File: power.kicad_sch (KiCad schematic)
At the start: 0 parts

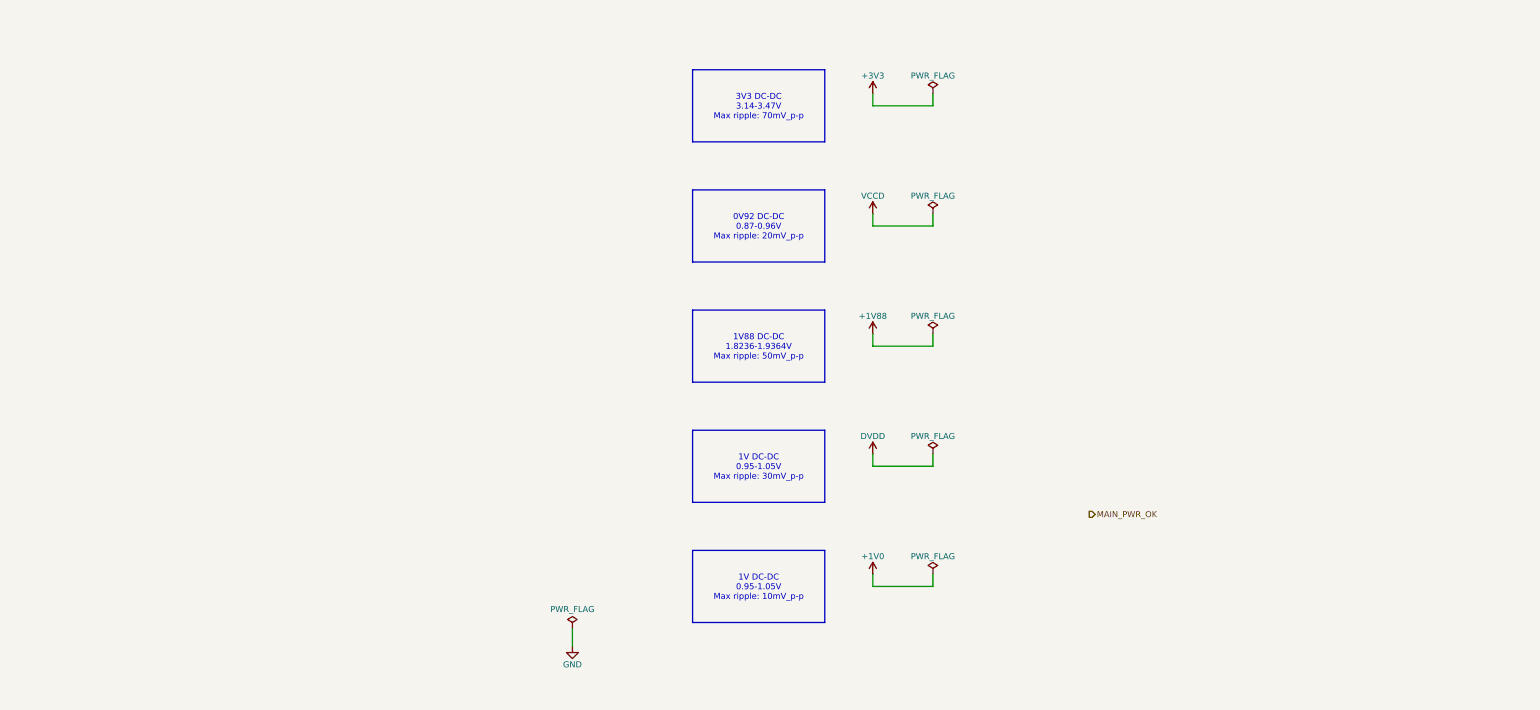
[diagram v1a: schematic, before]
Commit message: [#80813] Add power input connectors, heatsink, mounting, draft component placement
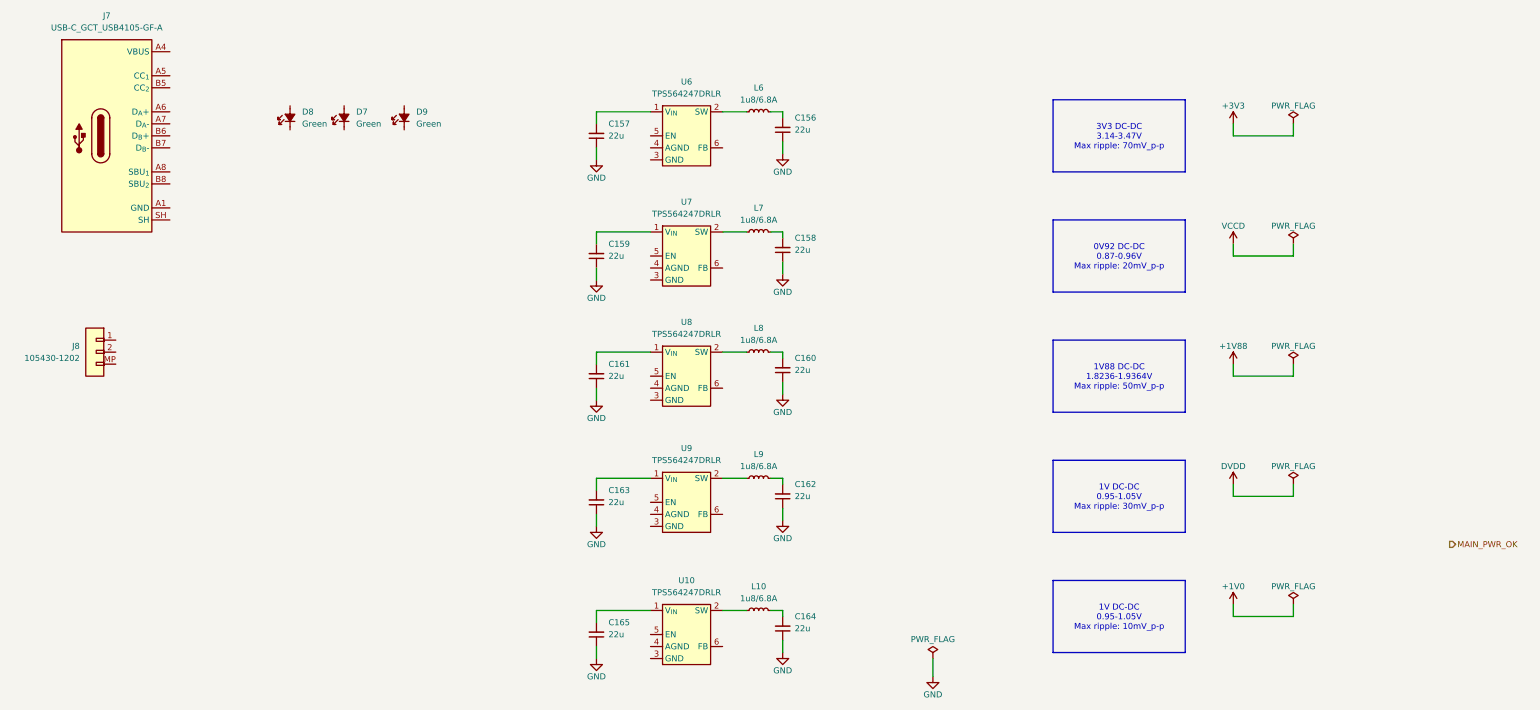
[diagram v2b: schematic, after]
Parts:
- added C156, C157, C158, C159, C160, C161, C162, C163, C164, C165: C_22u_16V_0603, antmicro-footprints:C_0603_1608Metric, symbol antmicroCapacitors0603:C_22u_16V_0603
- added D7, D8, D9: LED_G_0603_LG_L29K-G2J1-24-Z, antmicro-footprints:LED_0603_1608Metric_G, symbol antmicroLEDIndicationDiscrete:LED_G_0603_LG_L29K-G2J1-24-Z
- added J7: USB-C_GCT_USB4105-GF-A, antmicro-footprints:USB-C_Receptacle_GCT_USB4105-GF-A, symbol antmicroUSBConnectors:USB-C_GCT_USB4105-GF-A
- added J8: Molex_Nano-Fit_1x2_SMD_1054301202, antmicro-footprints:Conn_Molex_Nano-Fit_1x2_SMD_1054301202, symbol antmicroWire2BoardConnectors:Molex_Nano-Fit_1x2_SMD_1054301202
- added L10, L6, L7, L8, L9: L_1u8_6.8A_WE-MAPI-4020, antmicro-footprints:L_WE-MAPI-4020, symbol antmicroFixedInductors:L_1u8_6.8A_WE-MAPI-4020
- added U10, U6, U7, U8, U9: TPS564247DRLR, antmicro-footprints:SOT-563, symbol antmicroDCDCConverters:TPS564247DRLR
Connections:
- net GND: now also C156.1, C157.1, C158.1, C159.1, C160.1, C161.1, C162.1, C163.1, C164.1, C165.1
- new net: C156.2, L6.2
- new net: C162.2, L9.2
- new net: C165.2, U10.1 (V_{IN})
- new net: L10.1, U10.2 (SW)
- new net: L8.1, U8.2 (SW)
- new net: C160.2, L8.2
- new net: C159.2, U7.1 (V_{IN})
- new net: C161.2, U8.1 (V_{IN})
- new net: C157.2, U6.1 (V_{IN})
- new net: L6.1, U6.2 (SW)
- new net: L7.1, U7.2 (SW)
- new net: L9.1, U9.2 (SW)
- new net: C163.2, U9.1 (V_{IN})
- new net: C158.2, L7.2
- new net: C164.2, L10.2
- new net: J7.A1 (GND), J7.A12 (GND), J7.B1 (GND), J7.B12 (GND)
- new net: J7.A4 (VBUS), J7.A9 (VBUS), J7.B4 (VBUS), J7.B9 (VBUS)

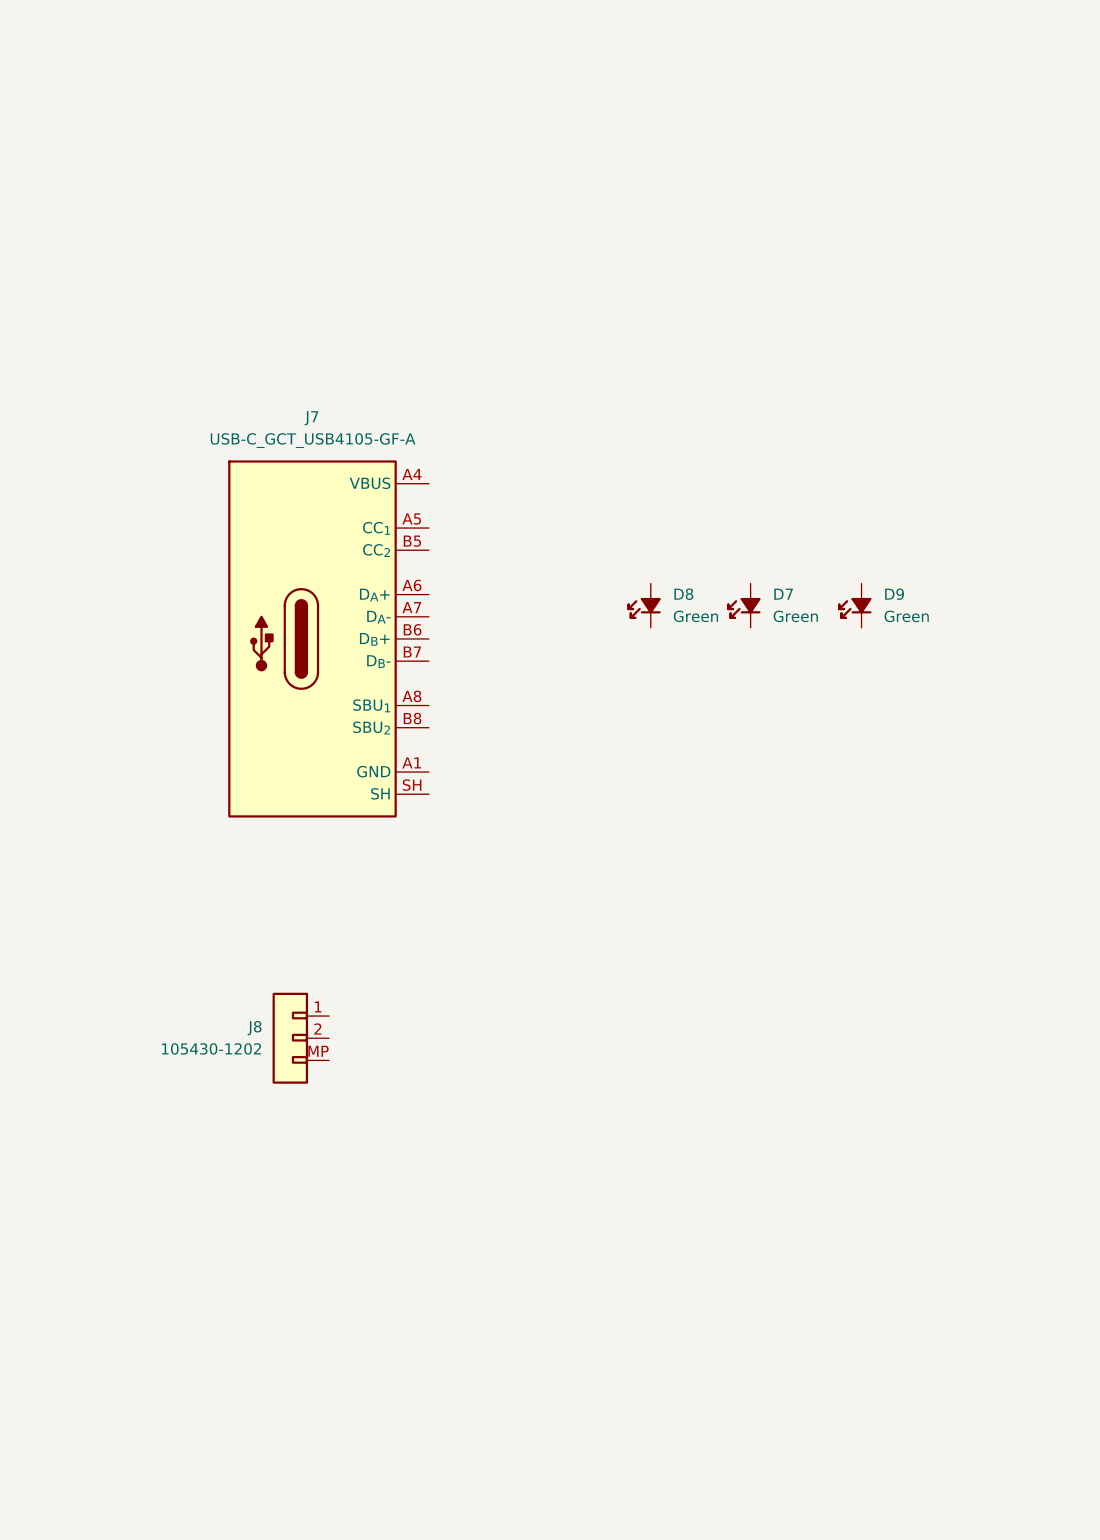
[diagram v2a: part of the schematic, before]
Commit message: [#80813] WIP: Connect USB-C connector
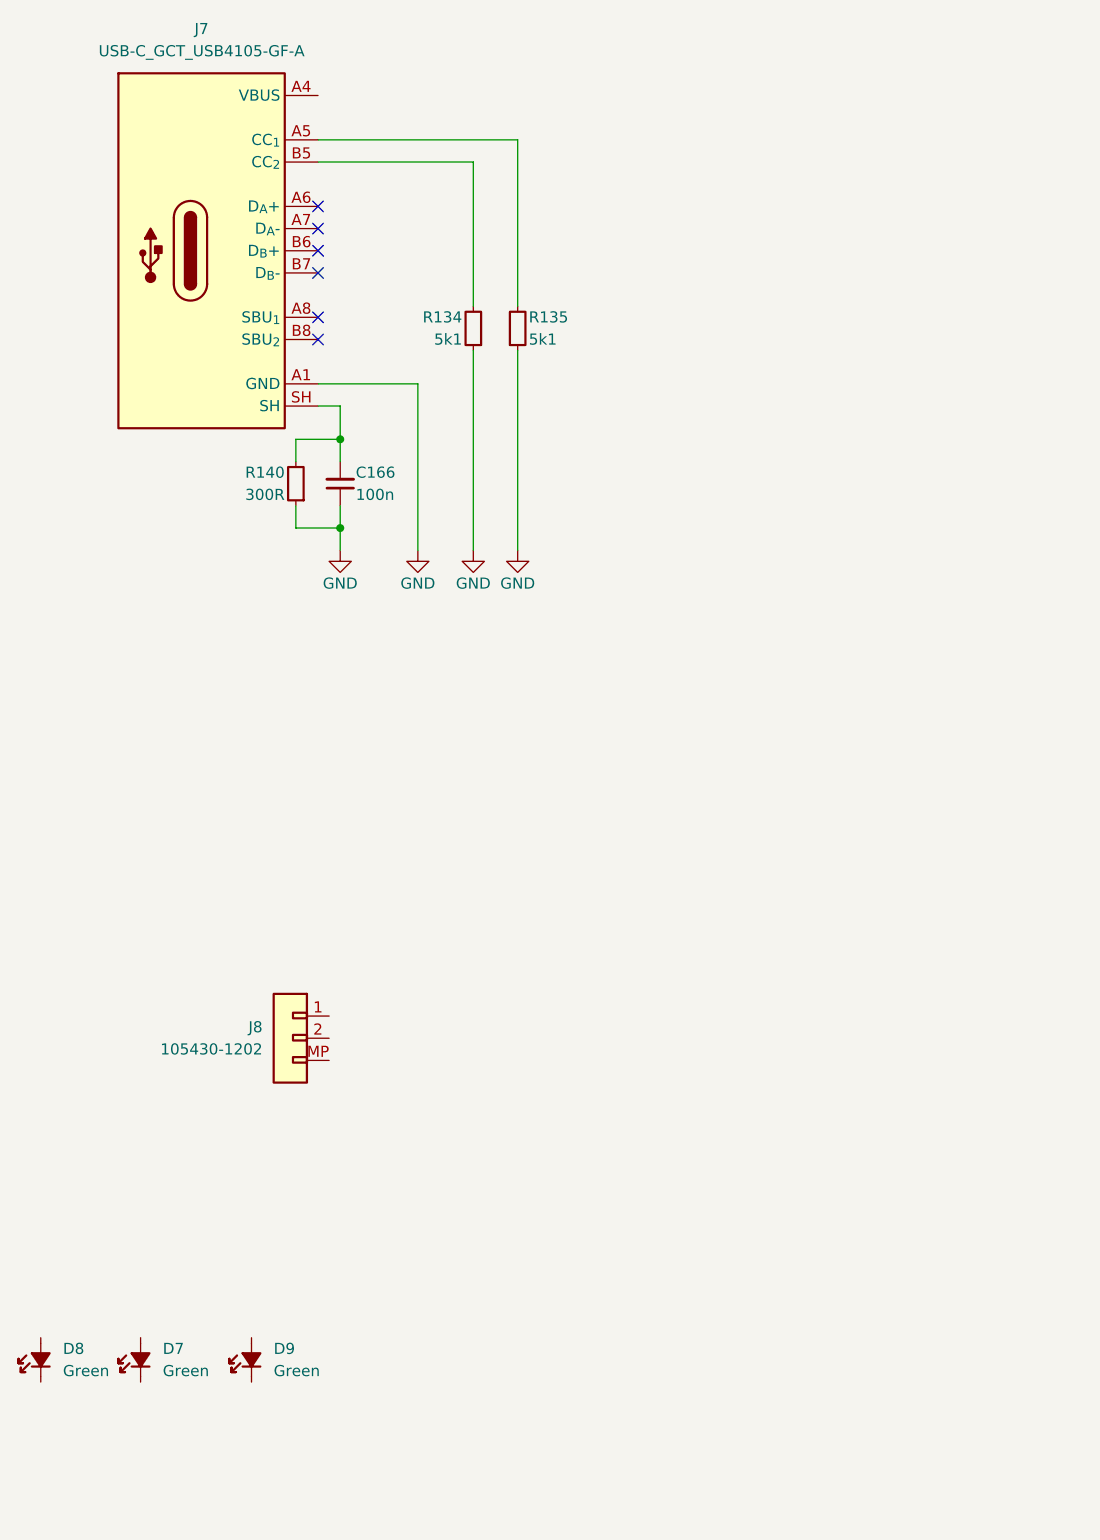
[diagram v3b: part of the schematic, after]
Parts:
- added C166: C_100n_16V_X7R_0402, antmicro-footprints:C_0402_1005Metric, symbol antmicroCapacitors0402:C_100n_16V_X7R_0402
- added R134, R135: R_5k1_0402, antmicro-footprints:R_0402_1005Metric, symbol antmicroResistors0402:R_5k1_0402
- added R140: R_300R_0402, antmicro-footprints:R_0402_1005Metric, symbol antmicroResistors0402:R_300R_0402
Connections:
- net GND: now also J7.A1 (GND), J7.A12 (GND), J7.B1 (GND), J7.B12 (GND), C166.1, R134.1, R135.1, R140.1
- net at J7.A5 (CC_{1}): now also R135.2
- net at J7.B5 (CC_{2}): now also R134.2
- net at J7.SH: now also C166.2, R140.2
- no-connect marks 0 -> 6
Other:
- moved on the sheet: D7, D8, D9, J7

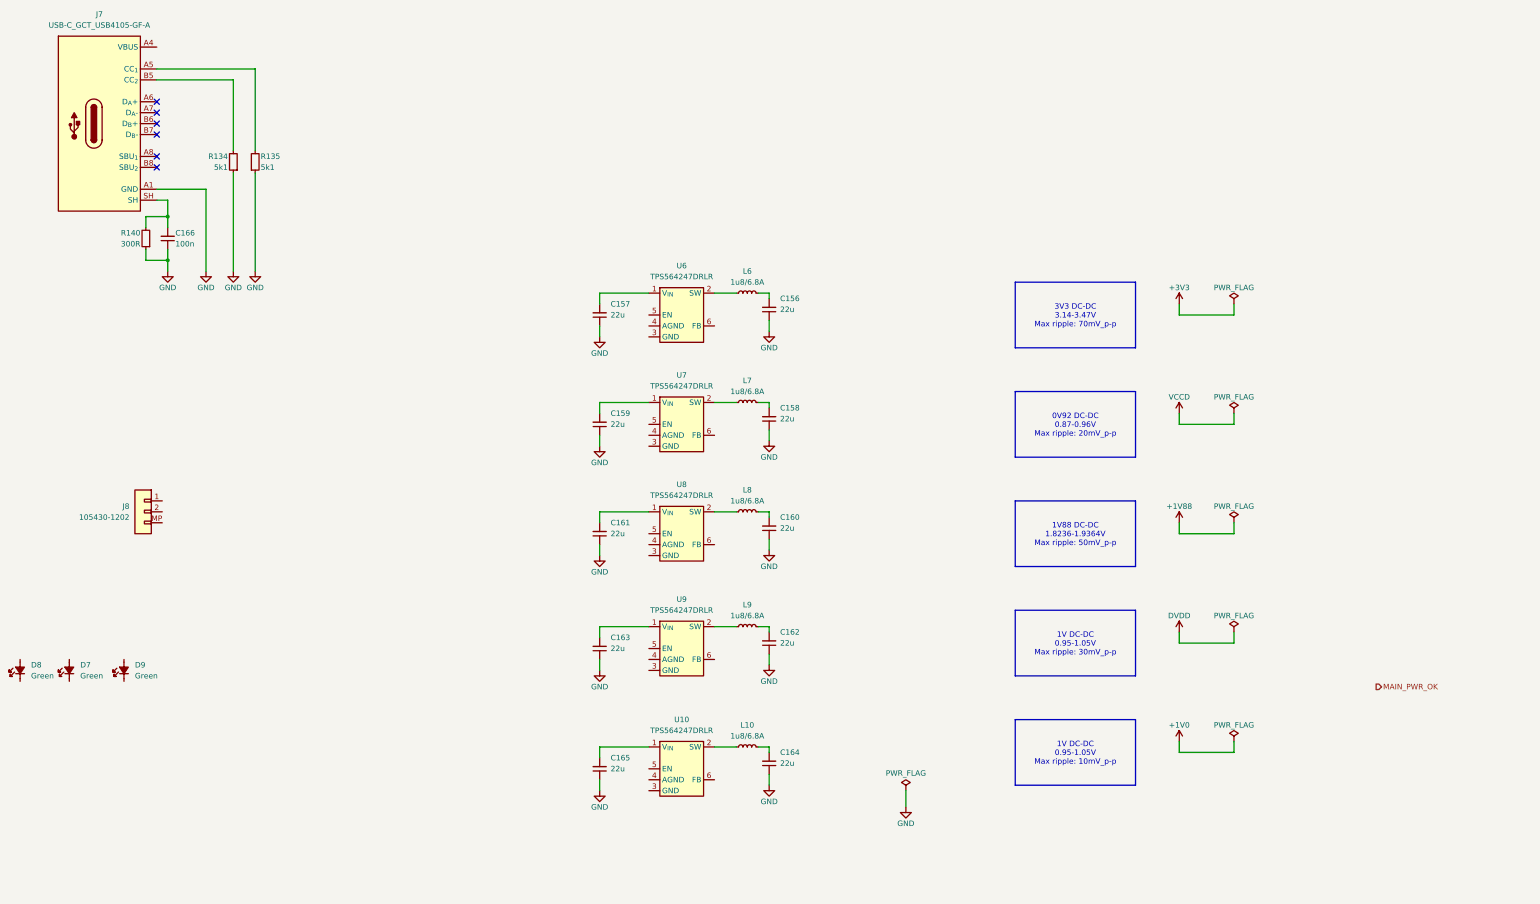
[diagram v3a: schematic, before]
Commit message: [#80813] Add power ORing
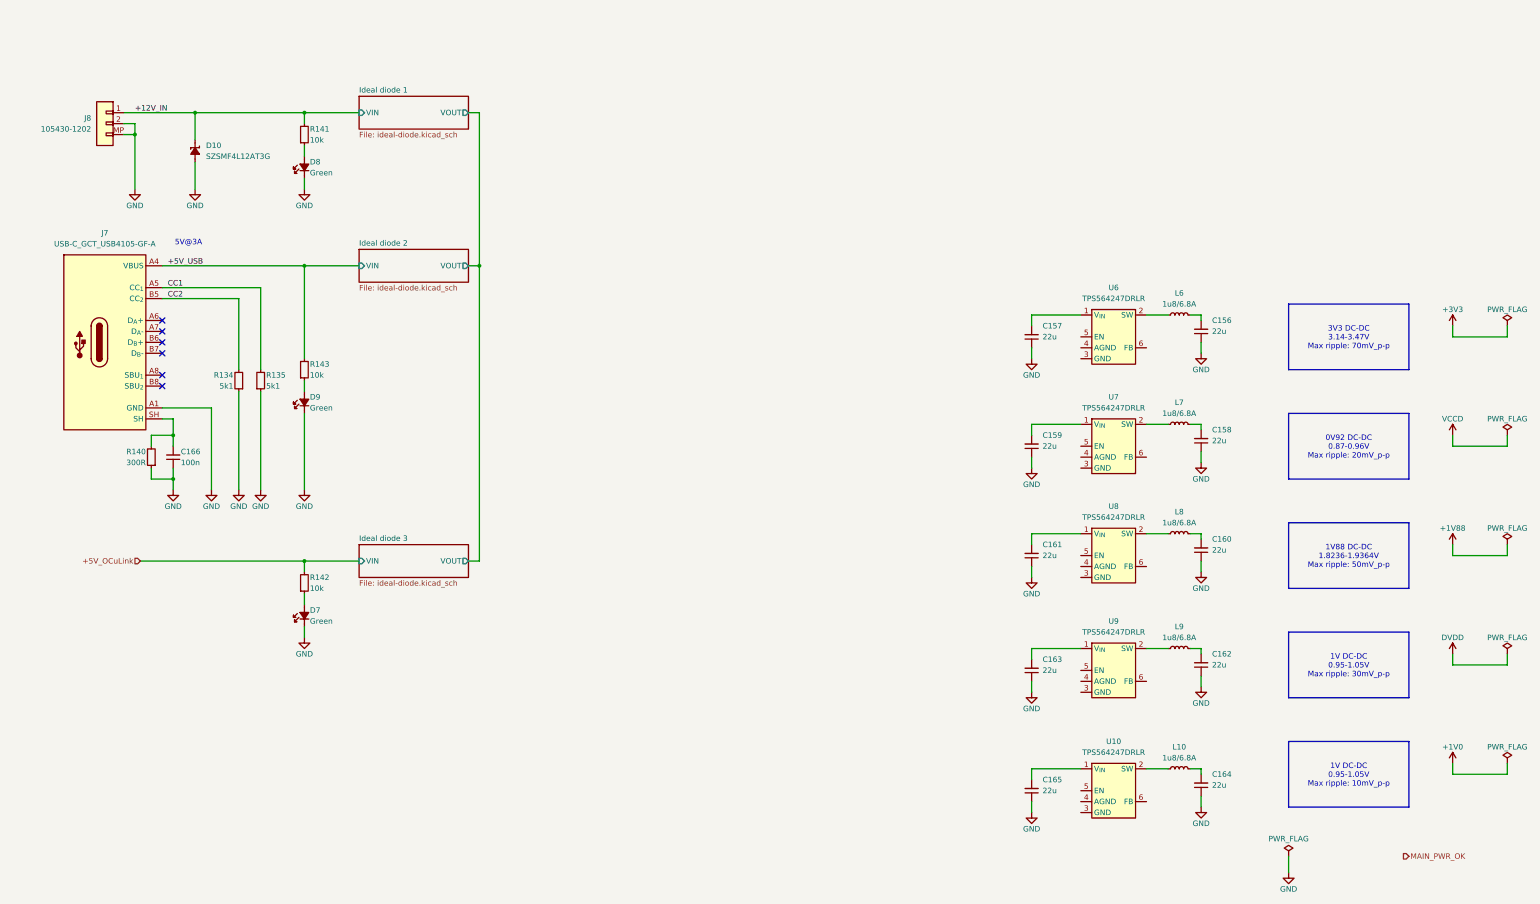
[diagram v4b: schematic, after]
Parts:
- added D10: SZSMF4L14AT3G, antmicro-footprints:SOD-123FL, symbol antmicroTVSDiodes:SZSMF4L14AT3G
- added R141, R142, R143: R_10k_0402, antmicro-footprints:R_0402_1005Metric, symbol antmicroResistors0402:R_10k_0402
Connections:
- net GND: now also D7.1 (C), D8.1 (C), D9.1 (C), J8.2, J8.MP, D10.2 (A)
- net at D8.2 (A): now also R141.1
- net CC2: now reaches J7.B5 (CC_{2}), R134.2
- net CC1: now reaches J7.A5 (CC_{1}), R135.2
- net at D7.2 (A): now also R142.1
- net at D9.2 (A): now also R143.1
- net +12V_IN: now reaches J8.1
- net +12V_IN: now also D10.1 (C), R141.2
- net +5V_USB: now reaches J7.A4 (VBUS), J7.A9 (VBUS), J7.B4 (VBUS), J7.B9 (VBUS)
- net +5V_USB: now also R143.2
- new net +5V_OCuLink: R142.2
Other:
- added sheet Ideal diode 1 (ideal-diode.kicad_sch)
- added sheet Ideal diode 2 (ideal-diode.kicad_sch)
- added sheet Ideal diode 3 (ideal-diode.kicad_sch)
- note added: "5V@3A"
- moved on the sheet: C156, C157, C158, C159, C160, C161, C162, C163, C164, C165, C166, D7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
